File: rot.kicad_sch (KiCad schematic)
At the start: 35 parts, among them J4 PinSocket_6x2_P2.54mm, J8 Molex_SlimStack_2x25_P0.5mm_5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, U2 W25Q32JV_SOIC-8, U3 W25Q32JV_SOIC-8, U4 W25Q32JV_SOIC-8, U5 W25Q32JV_SOIC-8

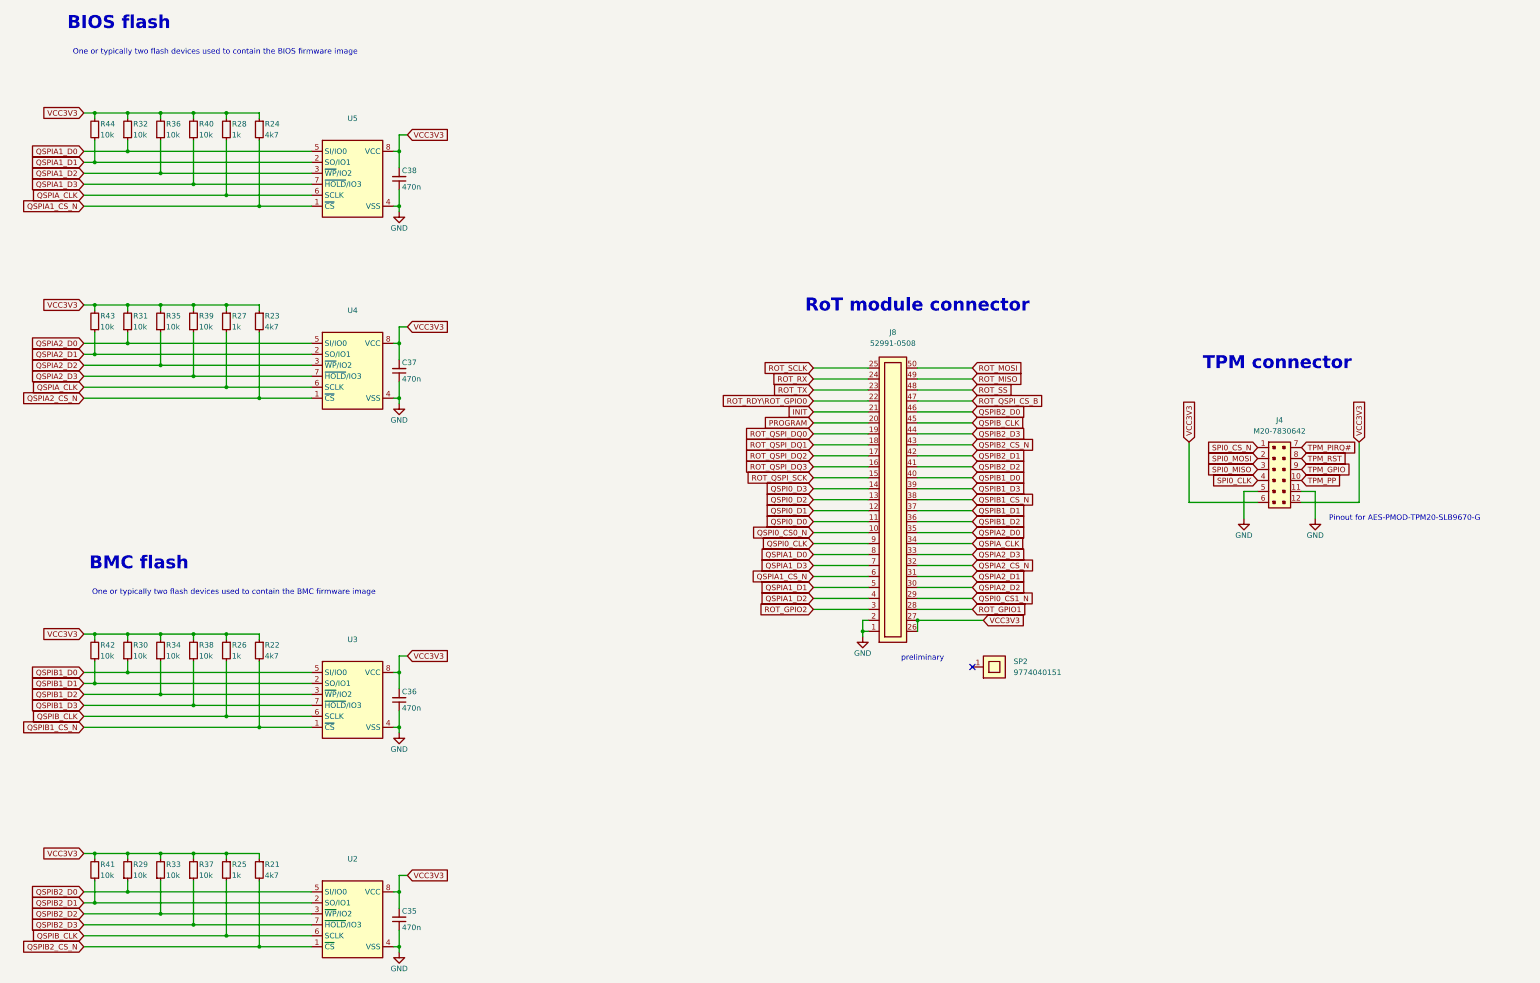
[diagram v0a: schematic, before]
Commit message: [#55652] Fix hotareas
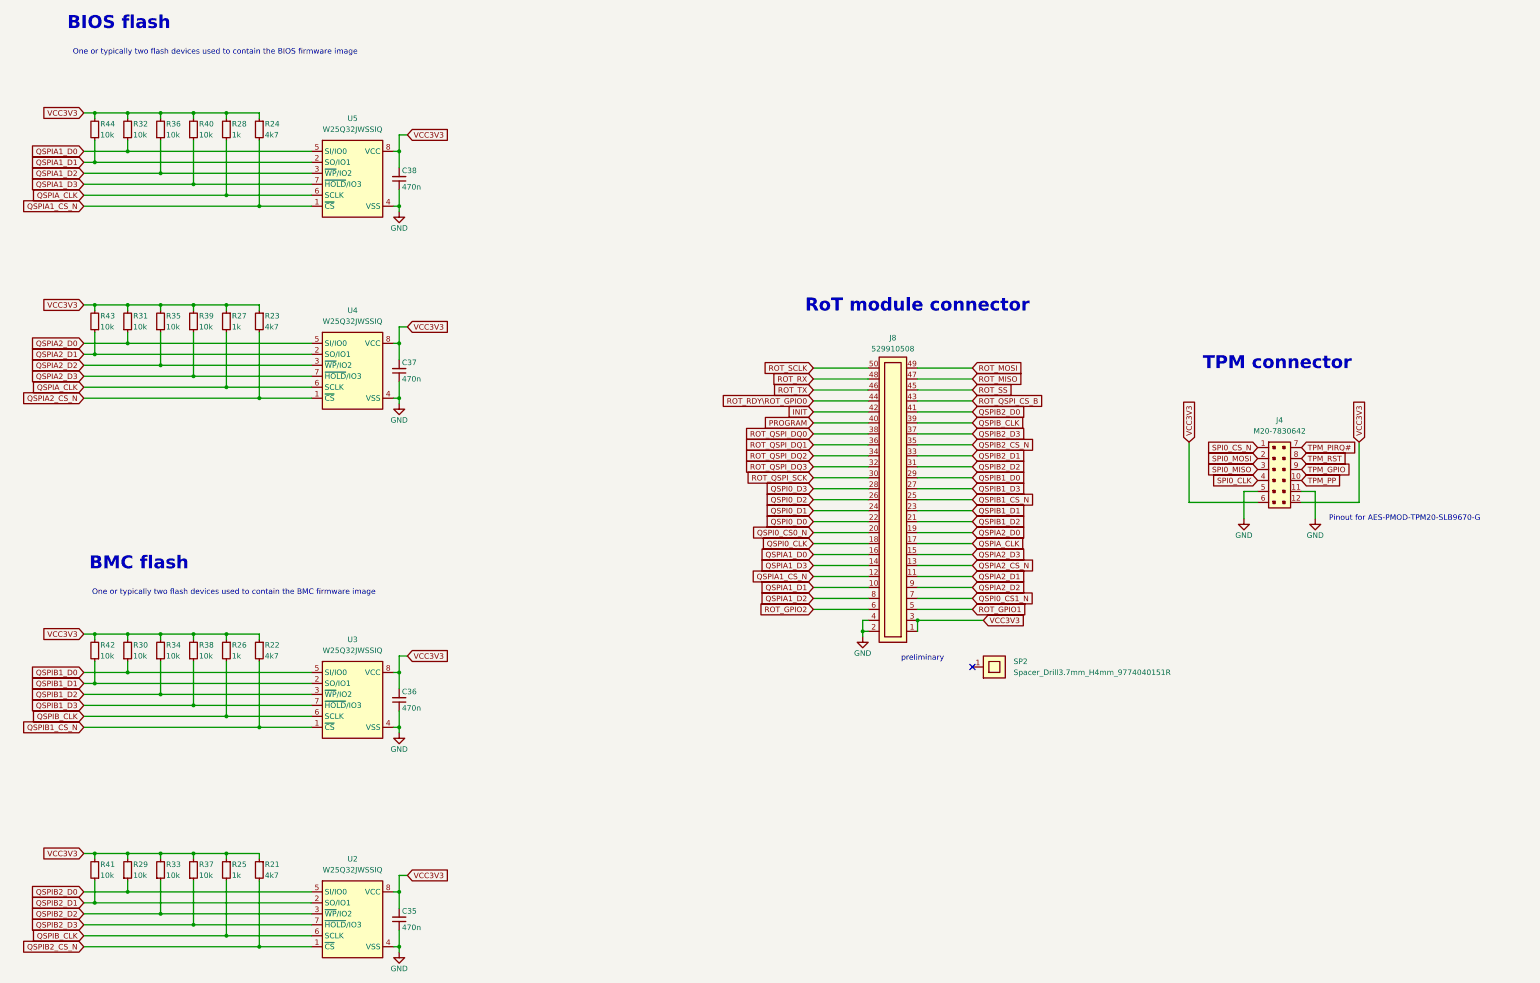
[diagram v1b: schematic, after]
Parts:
- J4: value PinSocket_6x2_P2.54mm -> PinSocket_2x6_P2.54mm_Drill1.02mm_PMOD; footprint antmicro-footprints:PinHeader_6x2_P2.54mm_Vertical_pmod -> antmicro-footprints:PinSocket_2x6_P2.54mm_Drill1.02mm_PMOD; symbol antmicroRectangularConnectorsHeadersFemalePins:PinSocket_6x2_P2.54mm -> antmicroGenericPinSockets:PinSocket_2x6_P2.54mm_Drill1.02mm_PMOD
- J8: value Molex_SlimStack_2x25_P0.5mm_529910-508 -> Plug_Molex_SlimStack_2x25_529910508; footprint antmicro-footprints:Conn_Molex_SlimStack_529910-508_2x25_P0.5mm -> antmicro-footprints:Conn_Plug_Molex_SlimStack_2x25_529910508; symbol antmicroB2bConnectors:Molex_SlimStack_2x25_P0.5mm_529910-508 -> antmicroB2BConnectors:Plug_Molex_SlimStack_2x25_529910508; MPN 52991-0508 -> 529910508; Pitch  (none) -> 0.5 mm
- SP2: value 9774040151 -> Spacer_Drill3.7mm_H4mm_9774040151R; footprint antmicro-footprints:9774040151 -> antmicro-footprints:Spacer_Drill3.7mm_H4mm_9774040151R; symbol antmicroMechanicalParts:9774040151 -> antmicroMechanicalParts:Spacer_Drill3.7mm_H4mm_9774040151R
- U2, U3, U4, U5: value W25Q32JV_SOIC-8 -> W25Q32JW_SOIC-8; footprint antmicro-footprints:SOIC-8-1EP_5.3x5.3x2mm_P1.27mm -> antmicro-footprints:SOIC-8_5.3x5.3x2mm_P1.27mm
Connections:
- net GND: now also J8.4; no longer J8.1
- net INIT: now also J8.42; no longer J8.21
- net PROGRAM: now also J8.40; no longer J8.20
- net QSPI0_CLK: now also J8.18; no longer J8.9
- net QSPI0_CS0_N: now also J8.20; no longer J8.10
- net QSPI0_CS1_N: now also J8.7; no longer J8.29
- net QSPI0_D0: now also J8.22; no longer J8.11
- net QSPI0_D1: now also J8.24; no longer J8.12
- net QSPI0_D2: now also J8.26; no longer J8.13
- net QSPI0_D3: now also J8.28; no longer J8.14
- net QSPIA1_CS_N: now also J8.12; no longer J8.6
- net QSPIA1_D0: now also J8.16; no longer J8.8
- net QSPIA1_D1: now also J8.10; no longer J8.5
- net QSPIA1_D2: now also J8.8; no longer J8.4
- net QSPIA1_D3: now also J8.14; no longer J8.7
- net QSPIA2_CS_N: now also J8.13; no longer J8.32
- net QSPIA2_D0: now also J8.19; no longer J8.35
- net QSPIA2_D1: now also J8.11; no longer J8.31
- net QSPIA2_D2: now also J8.9; no longer J8.30
- net QSPIA2_D3: now also J8.15; no longer J8.33
- net QSPIA_CLK: now also J8.17; no longer J8.34
- net QSPIB1_CS_N: now also J8.25; no longer J8.38
- net QSPIB1_D0: now also J8.29; no longer J8.40
- net QSPIB1_D1: now also J8.23; no longer J8.37
- net QSPIB1_D2: now also J8.21; no longer J8.36
- net QSPIB1_D3: now also J8.27; no longer J8.39
- net QSPIB2_CS_N: now also J8.35; no longer J8.43
- net QSPIB2_D0: now also J8.41; no longer J8.46
- net QSPIB2_D1: now also J8.33; no longer J8.42
- net QSPIB2_D2: now also J8.31; no longer J8.41
- net QSPIB2_D3: now also J8.37; no longer J8.44
- net QSPIB_CLK: now also J8.39; no longer J8.45
- net ROT_GPIO1: now also J8.5; no longer J8.28
- net ROT_GPIO2: now also J8.6; no longer J8.3
- net ROT_MISO: now also J8.47; no longer J8.49
- net ROT_MOSI: now also J8.49; no longer J8.50
- net ROT_QSPI_CS_B: now also J8.43; no longer J8.47
- net ROT_QSPI_DQ0: now also J8.38; no longer J8.19
- net ROT_QSPI_DQ1: now also J8.36; no longer J8.18
- net ROT_QSPI_DQ2: now also J8.34; no longer J8.17
- net ROT_QSPI_DQ3: now also J8.32; no longer J8.16
- net ROT_QSPI_SCK: now also J8.30; no longer J8.15
- net ROT_RDY\ROT_GPIO0: now also J8.44; no longer J8.22
- net ROT_RX: now also J8.48; no longer J8.24
- net ROT_SCLK: now also J8.50; no longer J8.25
- net ROT_SS: now also J8.45; no longer J8.48
- net ROT_TX: now also J8.46; no longer J8.23
- net VCC3V3: now also J8.1, J8.3; no longer J8.26, J8.27
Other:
- moved on the sheet: J8

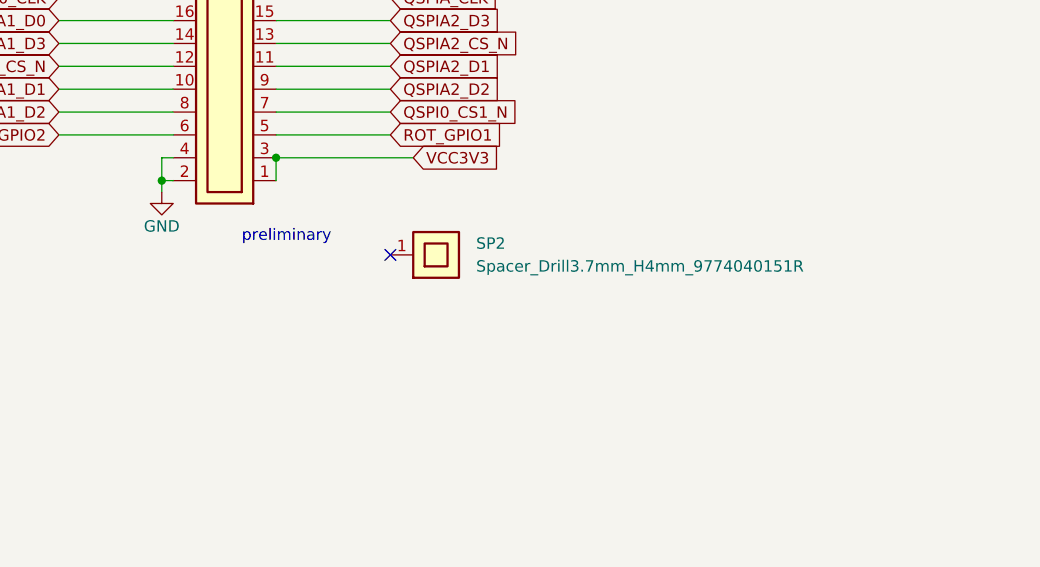
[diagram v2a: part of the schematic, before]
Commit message: [#68236] Change studs reference from SP to H
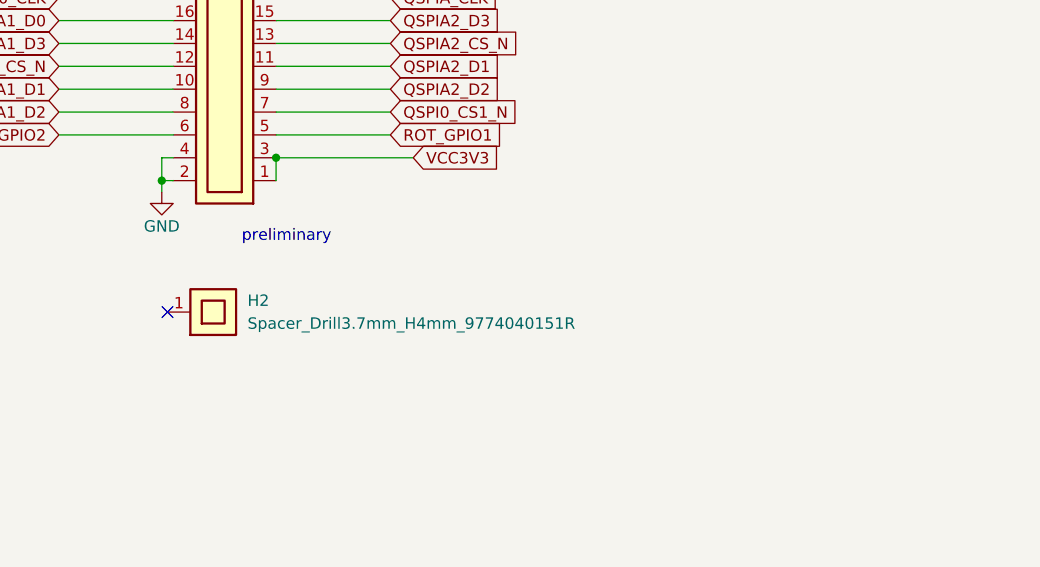
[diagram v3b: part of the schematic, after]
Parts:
- removed SP2: Spacer_Drill3.7mm_H4mm_9774040151R, antmicro-footprints:Spacer_Drill3.7mm_H4mm_9774040151R, symbol antmicroMechanicalParts:Spacer_Drill3.7mm_H4mm_9774040151R
- added H2: Spacer_Drill3.7mm_H4mm_9774040151R, antmicro-footprints:Spacer_Drill3.7mm_H4mm_9774040151R, symbol antmicroMechanicalParts:Spacer_Drill3.7mm_H4mm_9774040151R
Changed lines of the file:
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@@
   (junction (at 42.545 171.45) (diameter 0) (color 0 0 0 0)
   )
-  (no_connect (at 245.745 179.07))
+  (no_connect (at 220.98 185.42))
   (wire (pts (xy 221.615 160.655) (xy 208.915 160.655))
     (stroke (width 0) (type default))
@@
     )
   )
-  (symbol (lib_id "antmicroMechanicalParts:Spacer_Drill3.7mm_H4mm_9774040151R") (at 245.745 179.07 0) (unit 1)
-    (in_bom yes) (on_board yes) (dnp no) (fields_autoplaced)
-    (property "Reference" "SP2" (at 255.27 177.7999 0)
-      (effects (font (size 1.27 1.27)) (justify left))
-    )
-    (property "Value" "Spacer_Drill3.7mm_H4mm_9774040151R" (at 255.27 180.3399 0)
-      (effects (font (size 1.27 1.27) (thickness 0.15)) (justify left))
-    )
-    (property "Footprint" "antmicro-footprints:Spacer_Drill3.7mm_H4mm_9774040151R" (at 268.605 186.69 0)
-      (effects (font (size 1.27 1.27) (thickness 0.15)) (justify left bottom) hide)
-    )
-    (property "Datasheet" "https://www.we-online.com/components/products/datasheet/9774040151R.pdf" (at 268.605 189.23 0)
-      (effects (font (size 1.27 1.27) (thickness 0.15)) (justify left bottom) hide)
-    )
-    (property "Manufacturer" "Würth Elektronik" (at 268.605 191.77 0)
-      (effects (font (size 1.27 1.27) (thickness 0.15)) (justify left bottom) hide)
-    )
-    (property "MPN" "9774040151R" (at 268.605 194.31 0)
-      (effects (font (size 1.27 1.27) (thickness 0.15)) (justify left bottom) hide)
-    )
-    (property "Author" "Antmicro" (at 268.605 196.85 0)
-      (effects (font (size 1.27 1.27) (thickness 0.15)) (justify left bottom) hide)
-    )
-    (property "License" "Apache-2.0" (at 268.605 199.39 0)
-      (effects (font (size 1.27 1.27) (thickness 0.15)) (justify left bottom) hide)
-    )
-    (pin "1")
-    (instances
-      (project "artix-dc-scm"
-        (path "/f3cd042e-9a46-4397-9768-c62eb1c291be/00000000-0000-0000-0000-0000624c566f"
-          (reference "SP2") (unit 1)
-        )
-      )
-    )
-  )
   (symbol (lib_id "antmicropower:GND") (at 220.345 172.085 0) (mirror y) (unit 1)
     (in_bom yes) (on_board yes) (dnp no)
@@
         )
       )
+    )
+  )
+  (symbol (lib_name "Spacer_Drill3.7mm_H4mm_9774040151R_1") (lib_id "antmicroMechanicalParts:Spacer_Drill3.7mm_H4mm_9774040151R") (at 220.98 185.42 0) (unit 1)
+    (in_bom yes) (on_board yes) (dnp no) (fields_autoplaced)
+    (property "Reference" "H2" (at 229.87 184.15 0)
+      (effects (font (size 1.27 1.27) (thickness 0.15)) (justify left))
+    )
+    (property "Value" "Spacer_Drill3.7mm_H4mm_9774040151R" (at 229.87 186.69 0)
+      (effects (font (size 1.27 1.27) (thickness 0.15)) (justify left))
+    )
+    (property "Footprint" "antmicro-footprints:Spacer_Drill3.7mm_H4mm_9774040151R" (at 243.84 193.04 0)
+      (effects (font (size 1.27 1.27) (thickness 0.15)) (justify left bottom) hide)
+    )
+    (property "Datasheet" "https://www.we-online.com/components/products/datasheet/9774040151R.pdf" (at 243.84 195.58 0)
+      (effects (font (size 1.27 1.27) (thickness 0.15)) (justify left bottom) hide)
+    )
+    (property "Manufacturer" "Würth Elektronik" (at 243.84 198.12 0)
+      (effects (font (size 1.27 1.27) (thickness 0.15)) (justify left bottom) hide)
+    )
+    (property "MPN" "9774040151R" (at 243.84 200.66 0)
+      (effects (font (size 1.27 1.27) (thickness 0.15)) (justify left bottom) hide)
+    )
+    (property "Author" "Antmicro" (at 243.84 203.2 0)
+      (effects (font (size 1.27 1.27) (thickness 0.15)) (justify left bottom) hide)
+    )
+    (property "License" "Apache-2.0" (at 243.84 205.74 0)
+      (effects (font (size 1.27 1.27) (thickness 0.15)) (justify left bottom) hide)
+    )
+    (pin "1")
+    (instances
+      (project "artix-dc-scm"
+        (path "/f3cd042e-9a46-4397-9768-c62eb1c291be/00000000-0000-0000-0000-0000624c566f"
+          (reference "H2") (unit 1)
+        )
+      )
